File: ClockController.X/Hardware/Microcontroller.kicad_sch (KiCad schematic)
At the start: 3 parts, among them U1 PIC16F15224-I/SL

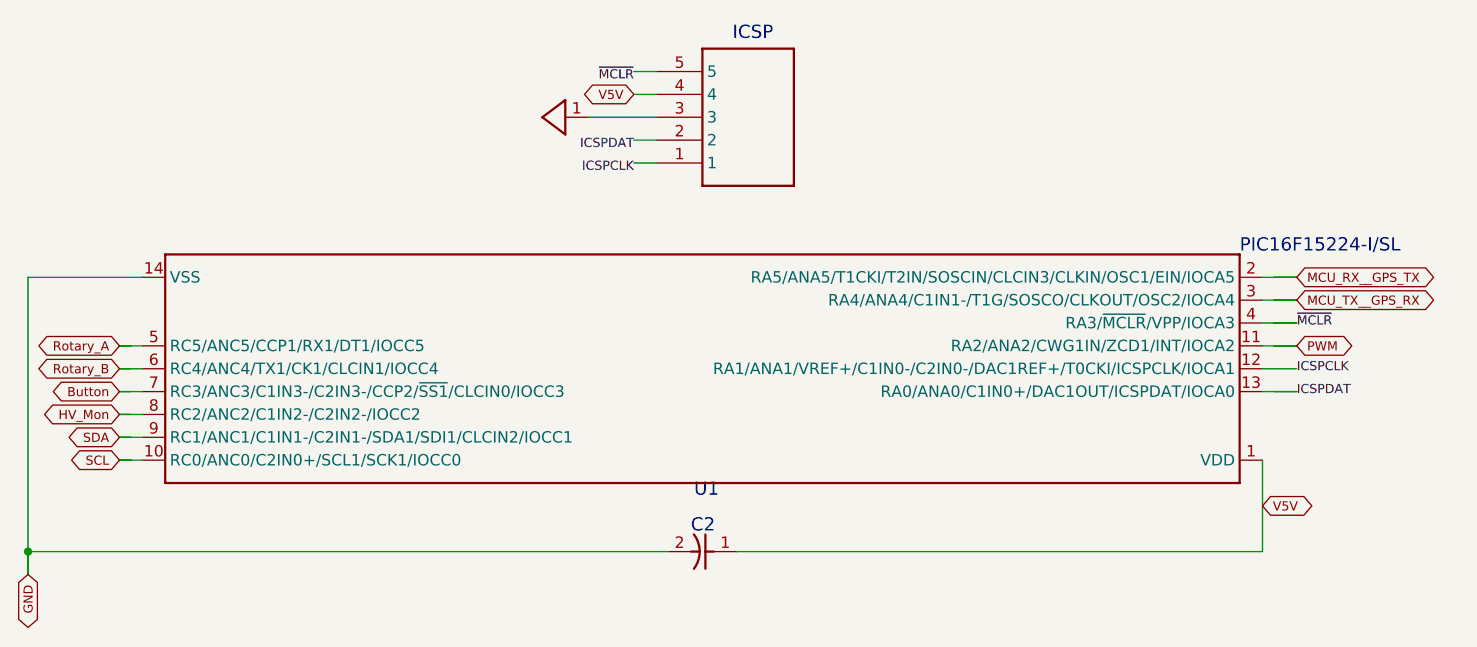
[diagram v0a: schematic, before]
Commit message: Fixed bad pull-up design of I2C cutoff transistors
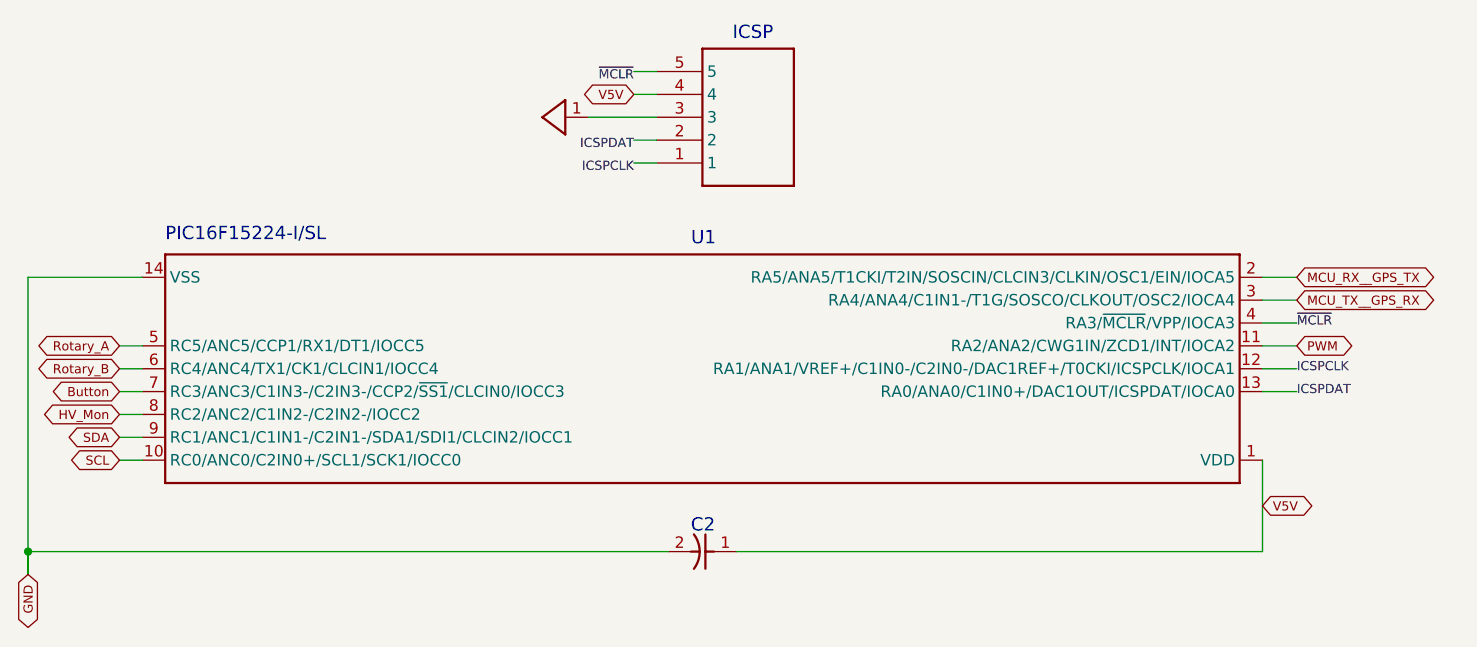
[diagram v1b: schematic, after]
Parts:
- U1: footprint Package_SO:SOIC-14_3.9x8.7mm_P1.27mm -> Clock Controller:SOIC14P127_869X599X175L84X42N; symbol Clock Controller-eagle-import:PIC16F15224-I/SL -> Clock Controller-eagle-import:PIC16F15225-I/SL
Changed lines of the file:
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@@
 	(text "PIC16F15224-I/SL"
 		(exclude_from_sim no)
-		(at 203.2 97.79 0)
+		(at 83.82 96.52 0)
 		(effects
 			(font
@@
 	(text "U1"
 		(exclude_from_sim no)
-		(at 142.581 123.19 0)
+		(at 142.24 95.25 0)
 		(effects
 			(font
@@
 	(wire
 		(pts
+			(xy 78.74 113.03) (xy 81.28 113.03)
+		)
+		(stroke
+			(width 0)
+			(type default)
+		)
+	)
+	(wire
+		(pts
+			(xy 205.74 105.41) (xy 209.55 105.41)
+		)
+		(stroke
+			(width 0)
+			(type default)
+		)
+	)
+	(wire
+		(pts
+			(xy 78.74 118.11) (xy 81.28 118.11)
+		)
+		(stroke
+			(width 0)
+			(type default)
+		)
+	)
+	(wire
+		(pts
 			(xy 68.58 130.81) (xy 68.58 100.33)
 		)
@@
 	(wire
 		(pts
-			(xy 78.74 115.57) (xy 80.01 115.57)
+			(xy 78.74 110.49) (xy 81.28 110.49)
+		)
+		(stroke
+			(width 0)
+			(type default)
+		)
+	)
+	(wire
+		(pts
+			(xy 135.89 80.01) (xy 138.43 80.01)
+		)
+		(stroke
+			(width 0)
+			(type default)
+		)
+	)
+	(wire
+		(pts
+			(xy 68.58 133.35) (xy 68.58 130.81)
 		)
 		(stroke
@@
 	(wire
 		(pts
-			(xy 209.55 100.33) (xy 207.01 100.33)
+			(xy 205.74 100.33) (xy 209.55 100.33)
+		)
+		(stroke
+			(width 0)
+			(type default)
+		)
+	)
+	(wire
+		(pts
+			(xy 68.58 133.35) (xy 68.58 130.81)
+		)
+		(stroke
+			(width 0)
+			(type default)
+		)
+	)
+	(wire
+		(pts
+			(xy 205.74 102.87) (xy 209.55 102.87)
+		)
+		(stroke
+			(width 0)
+			(type default)
+		)
+	)
+	(wire
+		(pts
+			(xy 135.89 87.63) (xy 138.43 87.63)
+		)
+		(stroke
+			(width 0)
+			(type default)
+		)
+	)
+	(wire
+		(pts
+			(xy 130.81 82.55) (xy 138.43 82.55)
+		)
+		(stroke
+			(width 0)
+			(type default)
+		)
+	)
+	(wire
+		(pts
+			(xy 205.74 130.81) (xy 147.32 130.81)
 		)
 		(stroke
@@
 	(wire
 		(pts
-			(xy 78.74 107.95) (xy 80.01 107.95)
+			(xy 205.74 113.03) (xy 209.55 113.03)
+		)
+		(stroke
+			(width 0)
+			(type default)
+		)
+	)
+	(wire
+		(pts
+			(xy 205.74 107.95) (xy 209.55 107.95)
+		)
+		(stroke
+			(width 0)
+			(type default)
+		)
+	)
+	(wire
+		(pts
+			(xy 78.74 120.65) (xy 81.28 120.65)
+		)
+		(stroke
+			(width 0)
+			(type default)
+		)
+	)
+	(wire
+		(pts
+			(xy 68.58 100.33) (xy 81.28 100.33)
 		)
 		(stroke
@@
 	(wire
 		(pts
-			(xy 209.55 110.49) (xy 205.74 110.49)
-		)
-		(stroke
-			(width 0)
-			(type default)
-		)
-	)
-	(wire
-		(pts
-			(xy 209.55 107.95) (xy 207.01 107.95)
+			(xy 78.74 115.57) (xy 81.28 115.57)
+		)
+		(stroke
+			(width 0)
+			(type default)
+		)
+	)
+	(wire
+		(pts
+			(xy 205.74 120.65) (xy 205.74 130.81)
 		)
 		(stroke
@@
 	(wire
 		(pts
-			(xy 78.74 110.49) (xy 80.01 110.49)
-		)
-		(stroke
-			(width 0.25)
-			(type solid)
-		)
-	)
-	(wire
-		(pts
-			(xy 78.74 113.03) (xy 81.28 113.03)
-		)
-		(stroke
-			(width 0)
-			(type default)
-		)
-	)
-	(wire
-		(pts
-			(xy 135.89 80.01) (xy 138.43 80.01)
-		)
-		(stroke
-			(width 0)
-			(type default)
-		)
-	)
-	(wire
-		(pts
-			(xy 209.55 102.87) (xy 207.01 102.87)
-		)
-		(stroke
-			(width 0.25)
-			(type solid)
-		)
-	)
-	(wire
-		(pts
-			(xy 68.58 133.35) (xy 68.58 130.81)
-		)
-		(stroke
-			(width 0.25)
-			(type solid)
-		)
-	)
-	(wire
-		(pts
-			(xy 78.74 118.11) (xy 81.28 118.11)
-		)
-		(stroke
-			(width 0)
-			(type default)
-		)
-	)
-	(wire
-		(pts
-			(xy 209.55 113.03) (xy 207.01 113.03)
-		)
-		(stroke
-			(width 0.25)
-			(type solid)
-		)
-	)
-	(wire
-		(pts
-			(xy 78.74 118.11) (xy 80.01 118.11)
-		)
-		(stroke
-			(width 0.25)
-			(type solid)
-		)
-	)
-	(wire
-		(pts
-			(xy 68.58 133.35) (xy 68.58 130.81)
-		)
-		(stroke
-			(width 0)
-			(type default)
-		)
-	)
-	(wire
-		(pts
-			(xy 209.55 107.95) (xy 205.74 107.95)
-		)
-		(stroke
-			(width 0)
-			(type default)
-		)
-	)
-	(wire
-		(pts
-			(xy 78.74 120.65) (xy 81.28 120.65)
-		)
-		(stroke
-			(width 0)
-			(type default)
-		)
-	)
-	(wire
-		(pts
-			(xy 135.89 87.63) (xy 138.43 87.63)
-		)
-		(stroke
-			(width 0)
-			(type default)
-		)
-	)
-	(wire
-		(pts
-			(xy 130.81 82.55) (xy 138.43 82.55)
-		)
-		(stroke
-			(width 0)
-			(type default)
-		)
-	)
-	(wire
-		(pts
-			(xy 205.74 130.81) (xy 147.32 130.81)
-		)
-		(stroke
-			(width 0.25)
-			(type solid)
-		)
-	)
-	(wire
-		(pts
-			(xy 209.55 105.41) (xy 205.74 105.41)
-		)
-		(stroke
-			(width 0)
-			(type default)
-		)
-	)
-	(wire
-		(pts
-			(xy 209.55 100.33) (xy 205.74 100.33)
-		)
-		(stroke
-			(width 0)
-			(type default)
-		)
-	)
-	(wire
-		(pts
-			(xy 209.55 113.03) (xy 205.74 113.03)
-		)
-		(stroke
-			(width 0)
-			(type default)
-		)
-	)
-	(wire
-		(pts
-			(xy 78.74 115.57) (xy 81.28 115.57)
-		)
-		(stroke
-			(width 0)
-			(type default)
-		)
-	)
-	(wire
-		(pts
-			(xy 78.74 120.65) (xy 80.01 120.65)
-		)
-		(stroke
-			(width 0.25)
-			(type solid)
-		)
-	)
-	(wire
-		(pts
-			(xy 68.58 100.33) (xy 81.28 100.33)
-		)
-		(stroke
-			(width 0.25)
-			(type solid)
-		)
-	)
-	(wire
-		(pts
-			(xy 209.55 105.41) (xy 207.01 105.41)
-		)
-		(stroke
-			(width 0.25)
-			(type solid)
-		)
-	)
-	(wire
-		(pts
 			(xy 78.74 107.95) (xy 81.28 107.95)
 		)
@@
 	(wire
 		(pts
-			(xy 209.55 102.87) (xy 205.74 102.87)
-		)
-		(stroke
-			(width 0)
-			(type default)
-		)
-	)
-	(wire
-		(pts
-			(xy 78.74 110.49) (xy 81.28 110.49)
-		)
-		(stroke
-			(width 0)
-			(type default)
-		)
-	)
-	(wire
-		(pts
-			(xy 205.74 120.65) (xy 205.74 130.81)
-		)
-		(stroke
-			(width 0.25)
-			(type solid)
-		)
-	)
-	(wire
-		(pts
-			(xy 78.74 113.03) (xy 80.01 113.03)
-		)
-		(stroke
-			(width 0.25)
-			(type solid)
+			(xy 205.74 110.49) (xy 209.55 110.49)
+		)
+		(stroke
+			(width 0)
+			(type default)
 		)
 	)
@@
 	)
 	(symbol
-		(lib_id "Clock Controller-eagle-import:PIC16F15224-I/SL")
+		(lib_id "Clock Controller-eagle-import:PIC16F15225-I/SL")
 		(at 143.51 110.49 180)
 		(unit 1)
@@
 			)
 		)
-		(property "Footprint" "Package_SO:SOIC-14_3.9x8.7mm_P1.27mm"
+		(property "Footprint" "Clock Controller:SOIC14P127_869X599X175L84X42N"
 			(at 143.51 110.49 0)
 			(effects
